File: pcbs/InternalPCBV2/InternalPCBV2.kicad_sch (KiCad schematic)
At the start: 24 parts, among them J1 JST-SH 1x3 SWD Debug, J2 USB_C_Receptacle, J3 USB Boot Switch, U1 RP2040, U2 NCP1117-3.3_SOT223, U3 W25Q128JVS

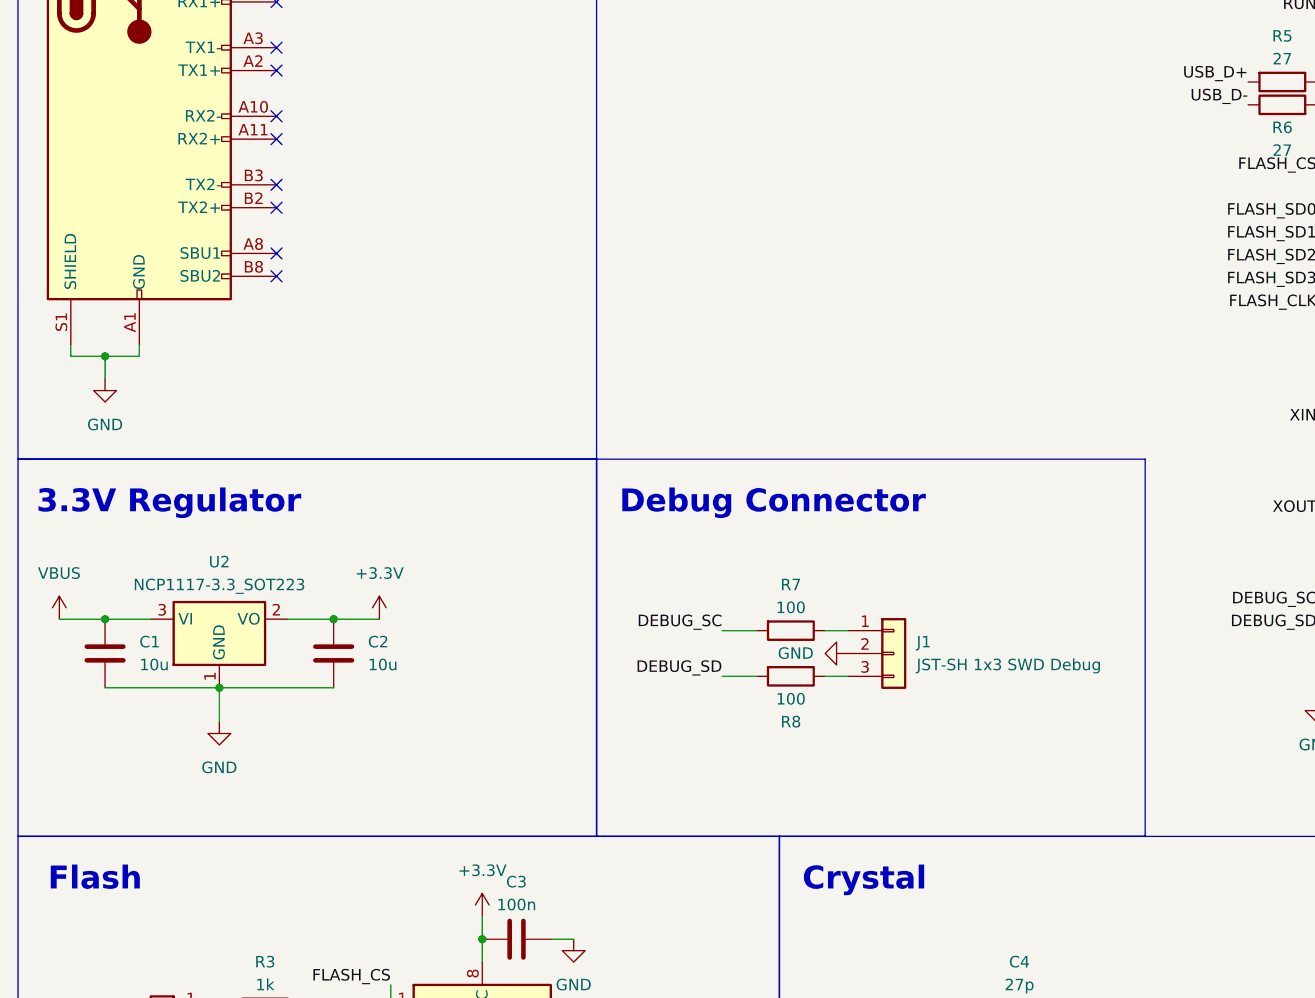
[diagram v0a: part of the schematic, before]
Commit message: Neue Datei für Display & RTC Chip(s)
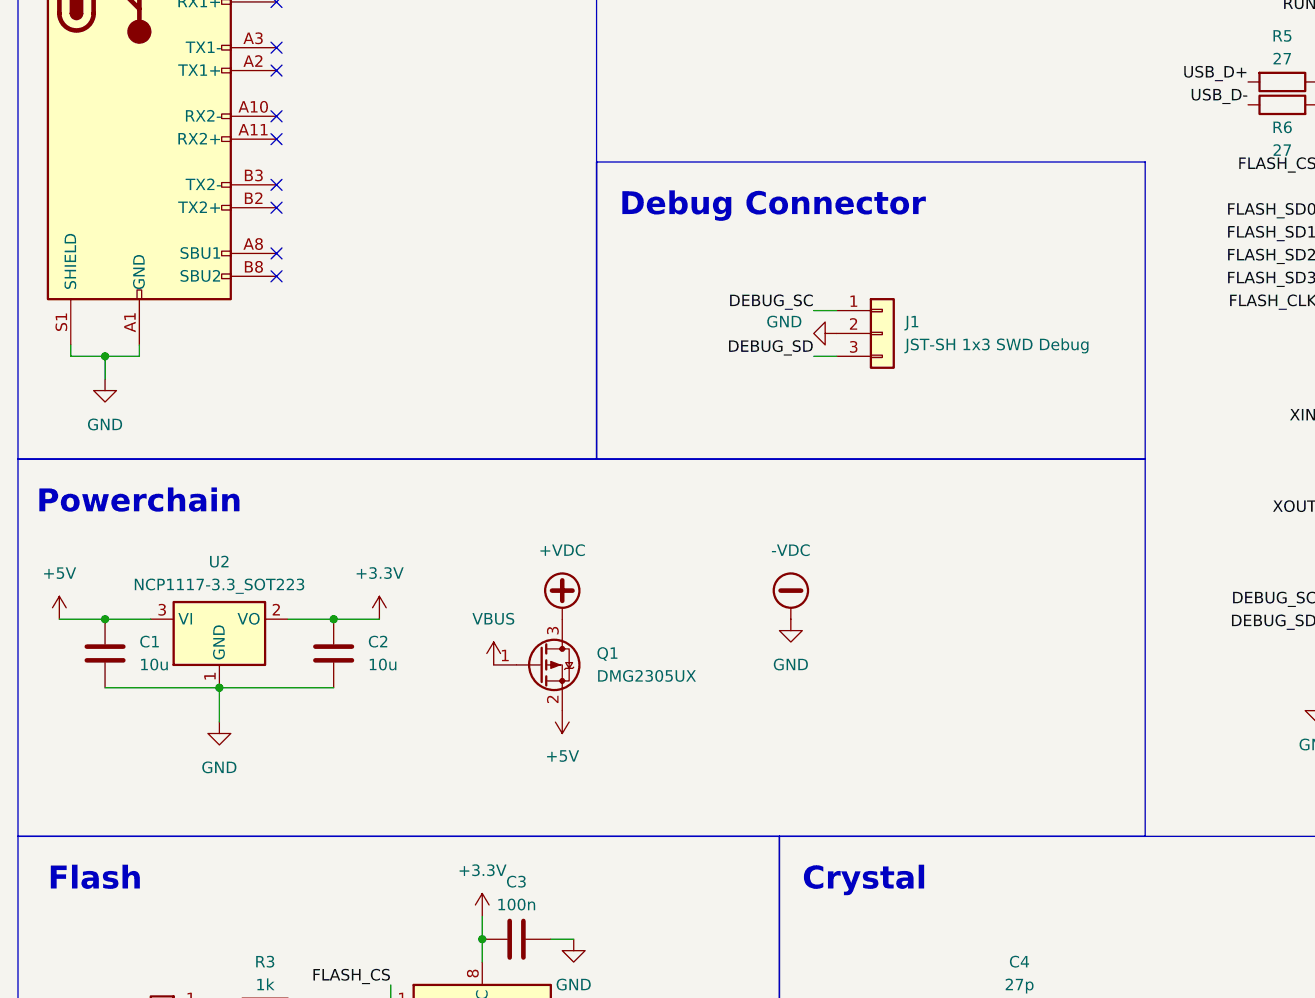
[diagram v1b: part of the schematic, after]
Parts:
- removed R7, R8: 100, Capacitor_SMD:C_0402_1005Metric, symbol Device:R
- added Q1: DMG2305UX, Package_TO_SOT_SMD:SOT-23, symbol Transistor_FET:DMG2301L
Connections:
- net DEBUG_SC: now also J1.1 (Pin_1)
- net DEBUG_SD: now also J1.3 (Pin_3)
- net VBUS: now also Q1.1 (G); no longer C1.1, U2.3 (VI)
- net GND renamed -VDC
- new net +5V: C1.1, Q1.2 (S), U2.3 (VI)
- new net +VDC: Q1.3 (D)
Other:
- note added: "Powerchain"
- note removed: "3.3V Regulator"
- moved on the sheet: J1

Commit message: Ein bisschen weitergespielt
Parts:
- added C11: C, symbol Device:C
- added Q2: DMG1012T, Package_TO_SOT_SMD:SOT-523, symbol Transistor_FET:DMG1012T
- added R7: 100k, symbol Device:R
- added R8: 200k, symbol Device:R
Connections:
- net +3.3V: now also Q2.1 (G)
- net +5V: now also R8.2
- net -VDC: now also C11.1, R7.1
- net VSYS_SENSE: now reaches U1.41 (GPIO29_ADC3)
- net VSYS_SENSE: now also Q2.2 (S)
- new net: C11.2, Q2.3 (D), R7.2, R8.1
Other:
- note added: "VSYS SENSE"

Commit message: Neuer Footprint für MH-Z19B/C CO2 Sensor
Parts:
- added J4: 694106301002, Connector_BarrelJack:BarrelJack_Wuerth_6941xx301002, symbol 694106301002:694106301002
- added R12, R13, R14, R15, R16, R17, R20, R21, R22, R23: 0, Resistor_SMD:R_0402_1005Metric, symbol Device:R
- C11: value C -> 1n; footprint (none) -> Capacitor_SMD:C_0402_1005Metric
- R1, R2, R3, R4, R5, R6: footprint Capacitor_SMD:C_0402_1005Metric -> Resistor_SMD:R_0402_1005Metric
- R7, R8: footprint (none) -> Resistor_SMD:R_0402_1005Metric
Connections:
- net I2C0_SCL: now also R21.2, R23.2; no longer U1.32 (GPIO21)
- net I2C0_SDA: now also R20.2, R22.2; no longer U1.31 (GPIO20)
- net GPIO_0: now reaches U1.2 (GPIO0)
- net GPIO_0: now also R22.1
- net TP_CS: now reaches U1.27 (GPIO16)
- net GPIO_18: now reaches U1.29 (GPIO18)
- net GPIO_18: now also R13.1
- net GPIO_1: now reaches U1.3 (GPIO1)
- net GPIO_1: now also R23.1
- net GPIO_19: now reaches U1.30 (GPIO19)
- net GPIO_19: now also R14.1
- net GPIO_5: now reaches U1.7 (GPIO5)
- net GPIO_5: now also R12.1
- net +VDC: no longer names the net of Q1.3 (D)
- net +VDC: now also J4.1 (POWER)
- net -VDC renamed GND
- net GND: now also J4.2 (GND_1), J4.3 (GND_2)
- net DISPLAY_IRQ renamed TP_IRQ
- new net GPIO_20: R15.1, R20.1
- new net GPIO_21: R16.1, R21.1
- new net GPIO_22: R17.1
- new net SDIO_CLK: R12.2
- new net SDIO_CMD: R13.2
- new net SDIO_D0: R14.2
- new net SDIO_D1: R15.2
- new net SDIO_D2: R16.2
- new net SDIO_D3CS: R17.2
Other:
- added sheet Sensors (Sensors.kicad_sch)
- moved on the sheet: C10, C6, C7, C9, Q1, R5, R6, U1
